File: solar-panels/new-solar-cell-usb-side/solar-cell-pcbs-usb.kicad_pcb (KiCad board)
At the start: 2 copper layers, 80 x 103.5 mm, 16 parts, among them J1 Solar Cell

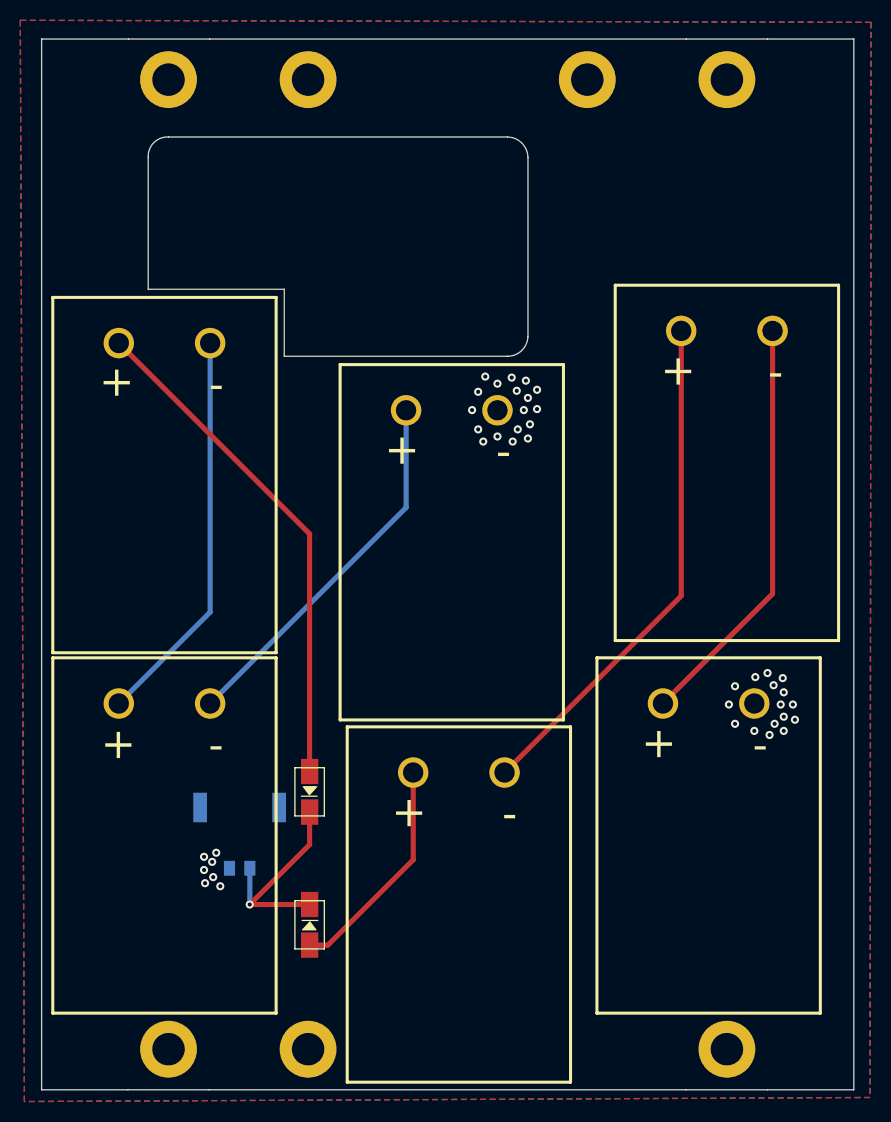
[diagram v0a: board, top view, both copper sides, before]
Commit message: fixed hole size and solar panel layout
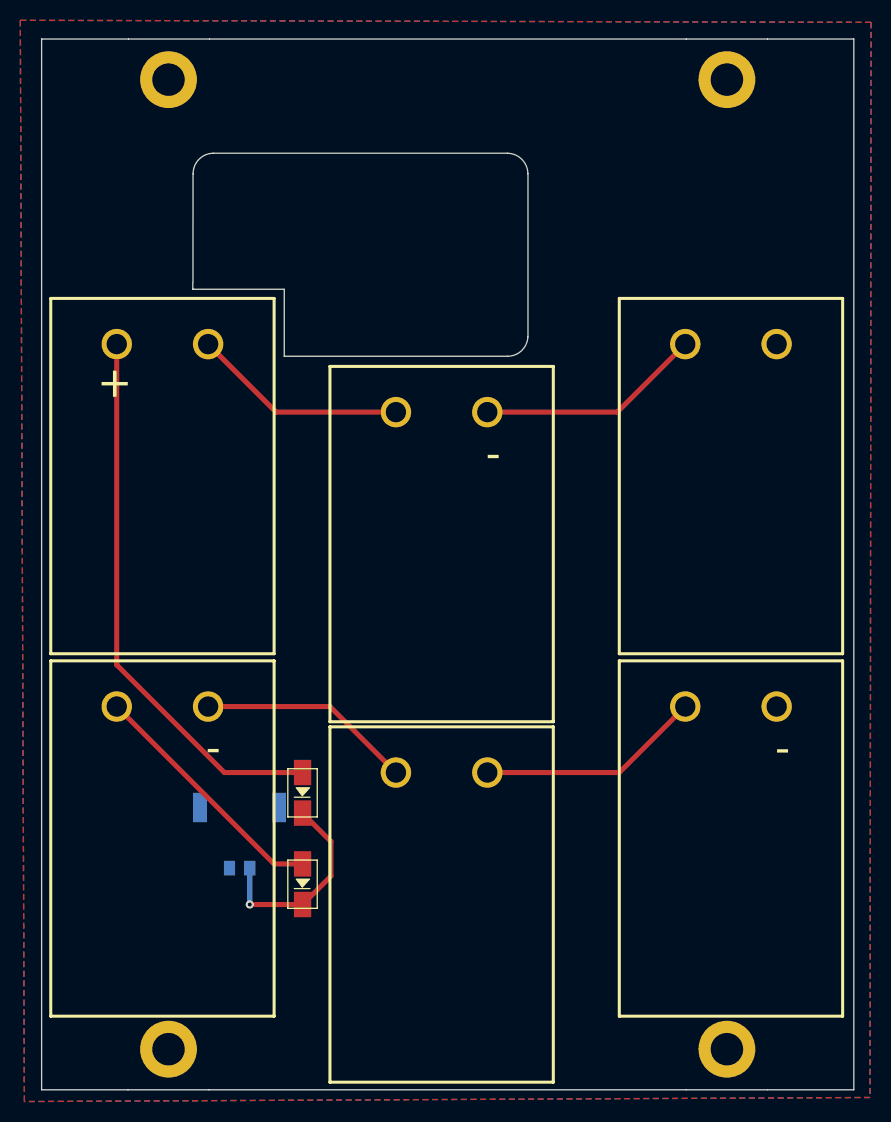
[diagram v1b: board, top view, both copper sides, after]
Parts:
- removed H2, H3, H6: MountingHole_Pad, MountingHole:MountingHole_3.2mm_M3_DIN965_Pad
- moved SC2 51.8 mm to (112.0, 124.0)
- moved SC5 39.6 mm to (112.0, 88.5)
- moved SC1 29.9 mm to (84.5, 117.5)
- moved SC6 28.3 mm to (140.5, 81.8)
- moved D1 4.06 mm to (97.8, 122.0), turned to 90 degrees
- moved SC3 2.22 mm to (140.5, 117.5)
- moved D2 0.71 mm to (97.8, 113.0)
- moved SC4 0.22 mm to (84.5, 81.8)
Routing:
- net Net-(SC1-Pad2): track 50.7 -> 21.2 mm
- net Net-(SC2-Pad2): track 41.2 -> 22.2 mm
- net Net-(SC4-Pad2): track 39.2 -> 21.3 mm
- net Net-(SC5-Pad2): track 36.9 -> 22.3 mm
- net Net-(D2-Pad2): track 50.0 -> 54.3 mm
- net Net-(D1-Pad2): track 22.3 -> 24.7 mm
- net VSOLAR: track 21.0 -> 20.1 mm
- net GND: vias 41 -> 0
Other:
- outline, holes or cut-outs redrawn
